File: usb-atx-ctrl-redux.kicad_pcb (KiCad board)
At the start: 2 copper layers, 24.2 x 48.9 mm, 16 parts, among them J1 Amphenol 54602-908LF, SW1 SX A08, SW2 SX A08, U1 AQW210EHA, U2 AQW210EHA

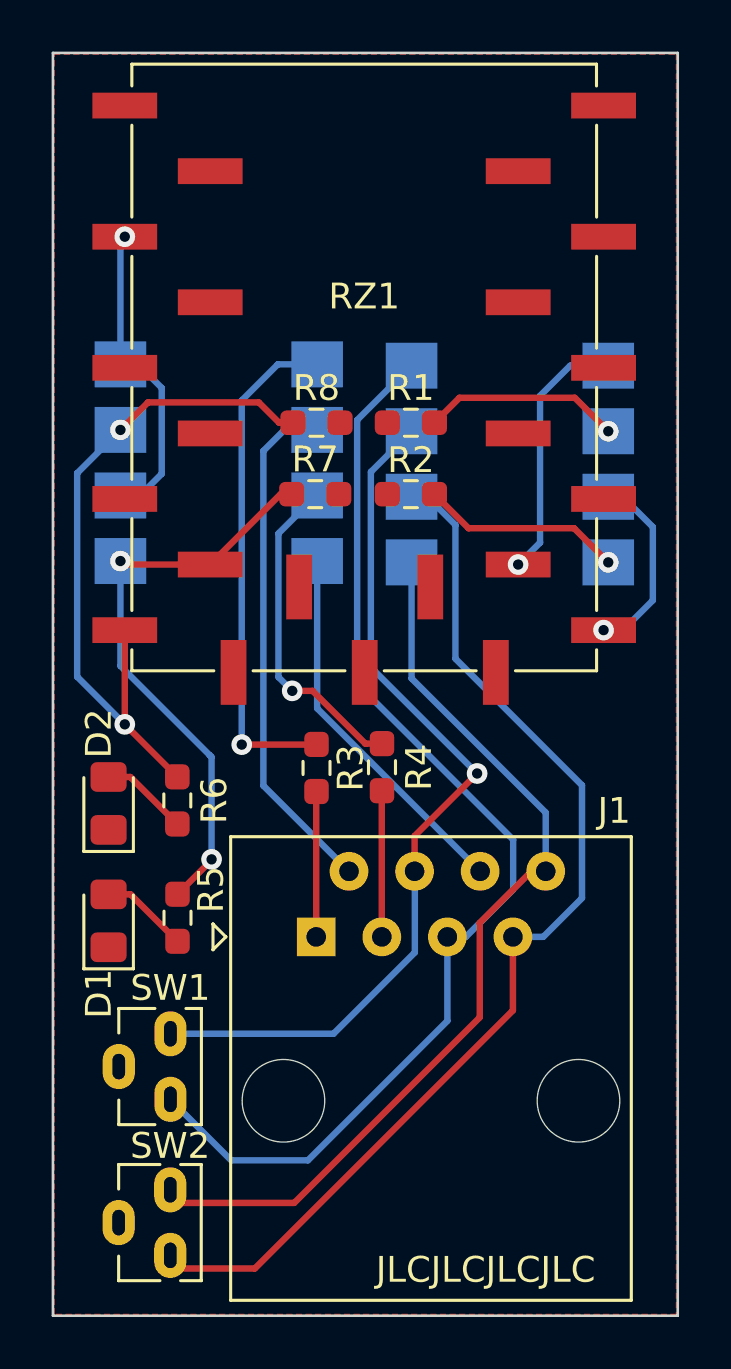
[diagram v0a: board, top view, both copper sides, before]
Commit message: Fix GPIO assignment, 8P8C footprint, bump to KiCad 8
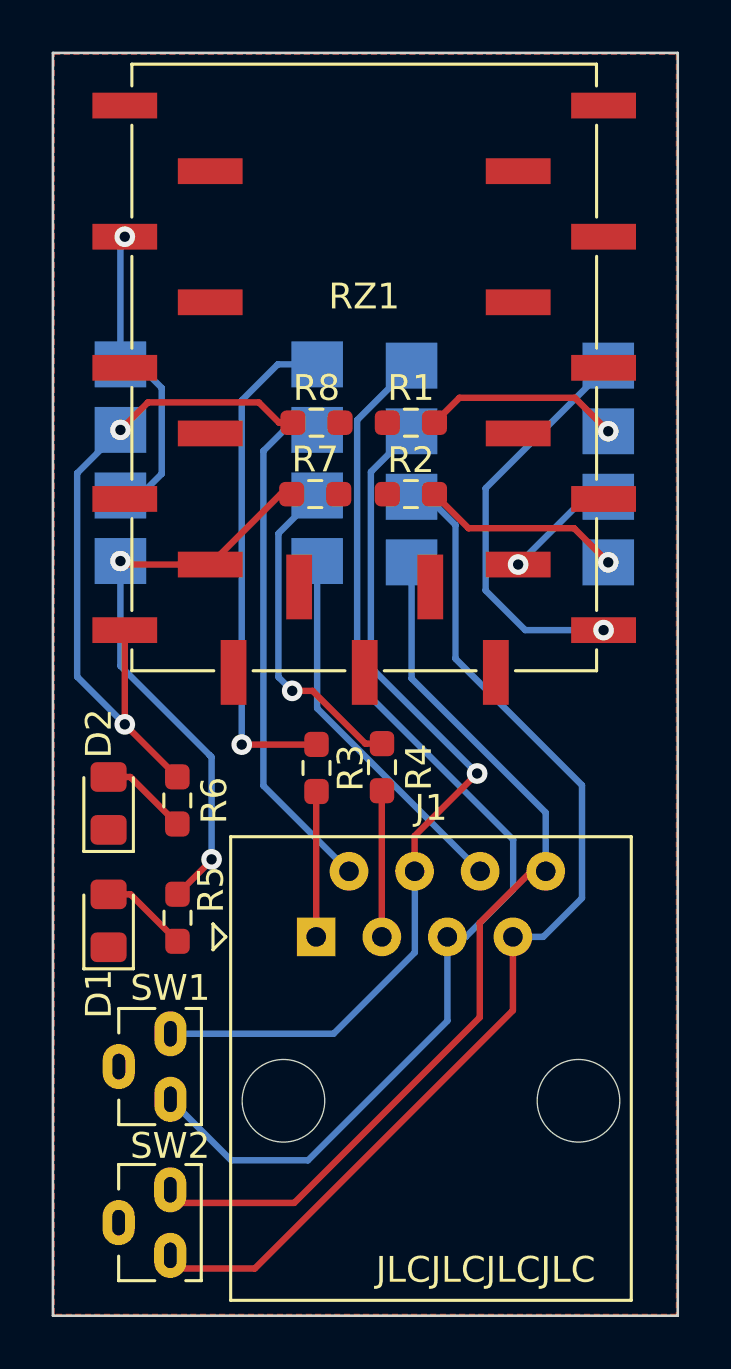
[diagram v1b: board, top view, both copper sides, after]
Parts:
- J1: footprint Connector_RJ:RJ45_Amphenol_54602-x08_Horizontal -> Custom_Parts:RJ45_Amphenol_54602-x08_Horizontal
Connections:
- RZ1 pad 8: /POWER -> /RESET
- RZ1 pad 9: /RESET -> /POWER
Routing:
- net /POWER: track 10.0 -> 15.9 mm
- net /RESET: track 7.44 -> 5.14 mm
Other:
- board text added: "usb-atx-ctrl redux Rev 0.2 (c) 2025 vmachinist"
- board text removed: "usb-atx-ctrl redux Rev 0.1 (c) 2023 vmachinist"
